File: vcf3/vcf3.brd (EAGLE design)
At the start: 58.4 x 216.8 mm, 100 parts, among them IC1 OPA4130P, IC2 OPA4130P, IC3 OPA134P, Q1 2N3904, Q10 2N3904, Q11 2N3904, Q12 2N3904, Q2 2N3904, Q3 2N3904, Q4 2N3904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

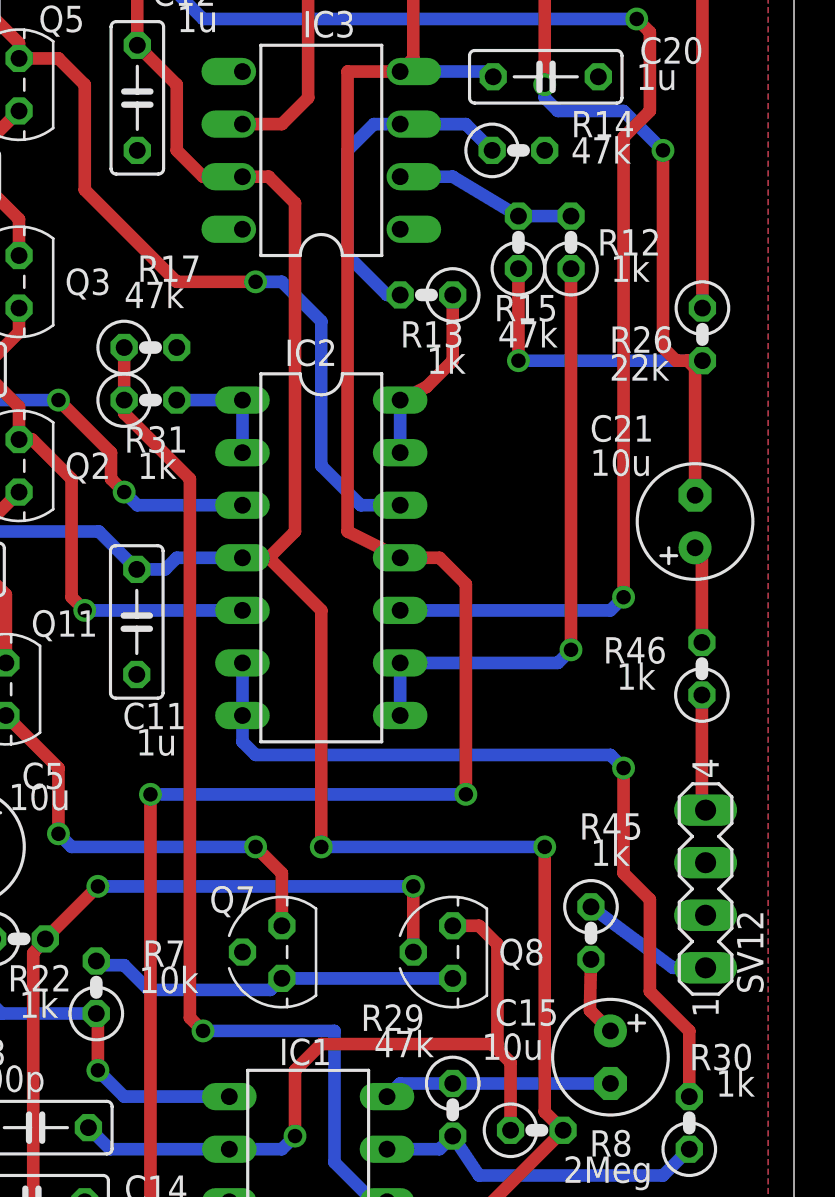
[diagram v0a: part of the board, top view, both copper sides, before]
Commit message: added tri and linear mod to vco, fixed serious errors with cvsource
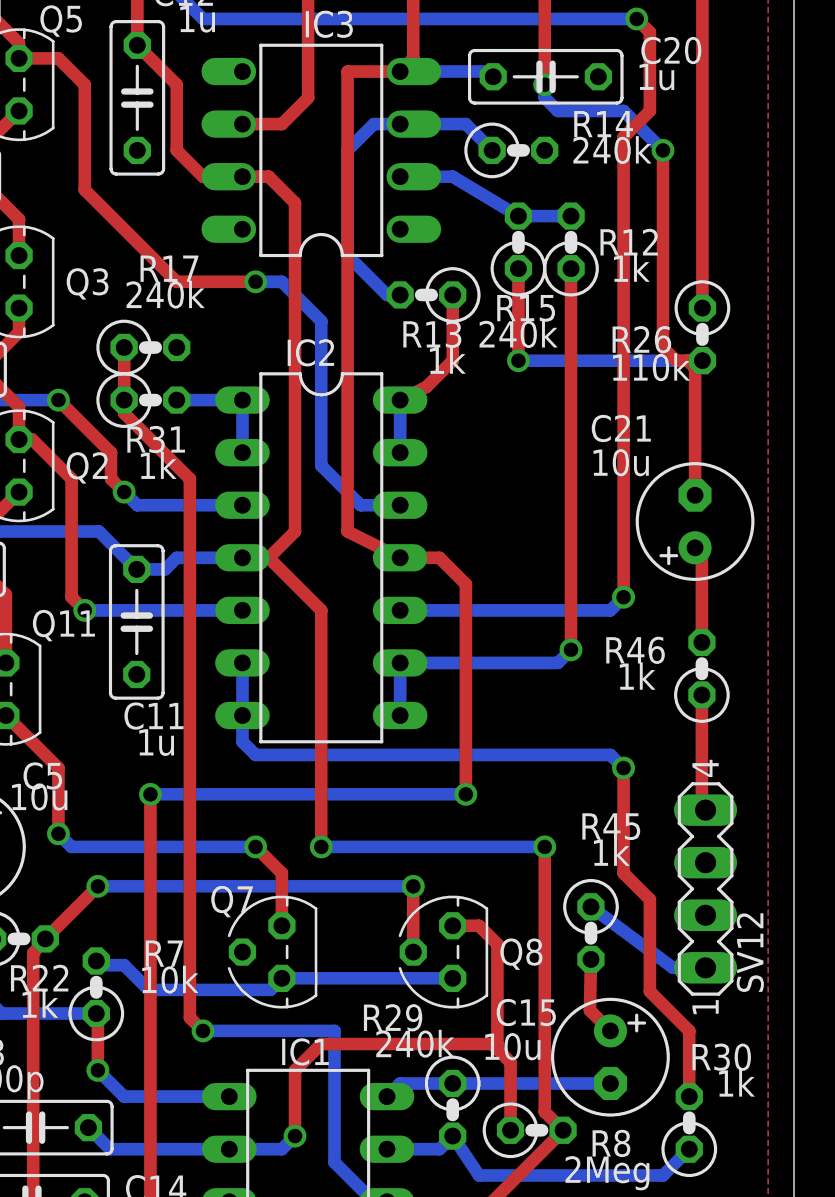
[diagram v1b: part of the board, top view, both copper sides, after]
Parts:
- R14, R15, R17, R29: value 47k -> 240k
- R26: value 22k -> 110k
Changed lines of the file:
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@@
 <attribute name="VALUE" x="40.64" y="61.595" size="1.27" layer="21" font="vector" ratio="15"/>
 </element>
-<element name="R14" library="dan" package="0207/2V" value="47k" x="45.085" y="72.39" smashed="yes">
+<element name="R14" library="dan" package="0207/2V" value="240k" x="45.085" y="72.39" smashed="yes">
 <attribute name="NAME" x="47.625" y="73.025" size="1.27" layer="21" font="vector" ratio="15"/>
 <attribute name="VALUE" x="47.625" y="71.755" size="1.27" layer="21" font="vector" ratio="15"/>
 </element>
-<element name="R15" library="dan" package="0207/2V" value="47k" x="45.085" y="67.945" smashed="yes" rot="R90">
+<element name="R15" library="dan" package="0207/2V" value="240k" x="45.085" y="67.945" smashed="yes" rot="R90">
 <attribute name="NAME" x="46.99" y="65.405" size="1.27" layer="21" font="vector" ratio="15" rot="R180"/>
 <attribute name="VALUE" x="46.99" y="64.135" size="1.27" layer="21" font="vector" ratio="15" rot="R180"/>
@@
 <attribute name="VALUE" x="15.875" y="34.29" size="1.27" layer="21" font="vector" ratio="15" rot="R180"/>
 </element>
-<element name="R17" library="dan" package="0207/2V" value="47k" x="27.305" y="62.865" smashed="yes">
+<element name="R17" library="dan" package="0207/2V" value="240k" x="27.305" y="62.865" smashed="yes">
 <attribute name="NAME" x="26.67" y="66.04" size="1.27" layer="21" font="vector" ratio="15"/>
 <attribute name="VALUE" x="26.035" y="64.77" size="1.27" layer="21" font="vector" ratio="15"/>
@@
 <attribute name="VALUE" x="28.3422" y="189.3566" size="1.27" layer="21" font="vector" ratio="15"/>
 </element>
-<element name="R29" library="dan" package="0207/2V" value="47k" x="41.91" y="26.035" smashed="yes" rot="R270">
+<element name="R29" library="dan" package="0207/2V" value="240k" x="41.91" y="26.035" smashed="yes" rot="R270">
 <attribute name="NAME" x="37.465" y="29.845" size="1.27" layer="21" font="vector" ratio="15"/>
 <attribute name="VALUE" x="38.1" y="28.575" size="1.27" layer="21" font="vector" ratio="15"/>
@@
 <attribute name="VALUE" x="4.0894" y="28.829" size="1.27" layer="21" font="vector" ratio="15"/>
 </element>
-<element name="R26" library="dan" package="0207/2V" value="22k" x="53.975" y="63.5" smashed="yes" rot="R270">
+<element name="R26" library="dan" package="0207/2V" value="110k" x="53.975" y="63.5" smashed="yes" rot="R270">
 <attribute name="NAME" x="49.4792" y="62.611" size="1.27" layer="21" font="vector" ratio="15"/>
 <attribute name="VALUE" x="49.4792" y="61.2648" size="1.27" layer="21" font="vector" ratio="15"/>
